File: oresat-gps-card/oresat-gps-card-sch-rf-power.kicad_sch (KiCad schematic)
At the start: 29 parts, among them U15 SKY65723-81, U16 BP2G+, U17 MAX8510EXK29+T, U18 MAX8510EXK29+T, U19 MAX8510EXK33+T

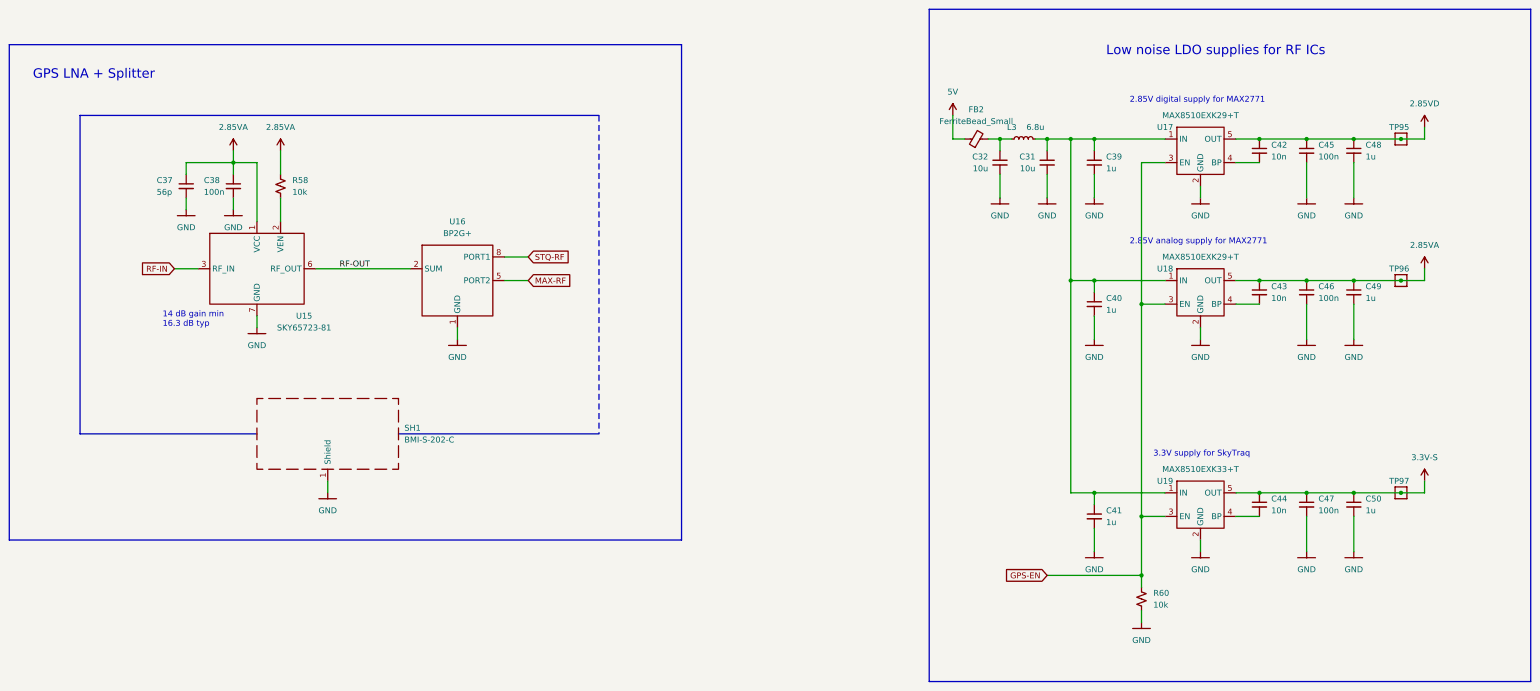
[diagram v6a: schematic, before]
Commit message: updated symbols and started new 2771 symbol
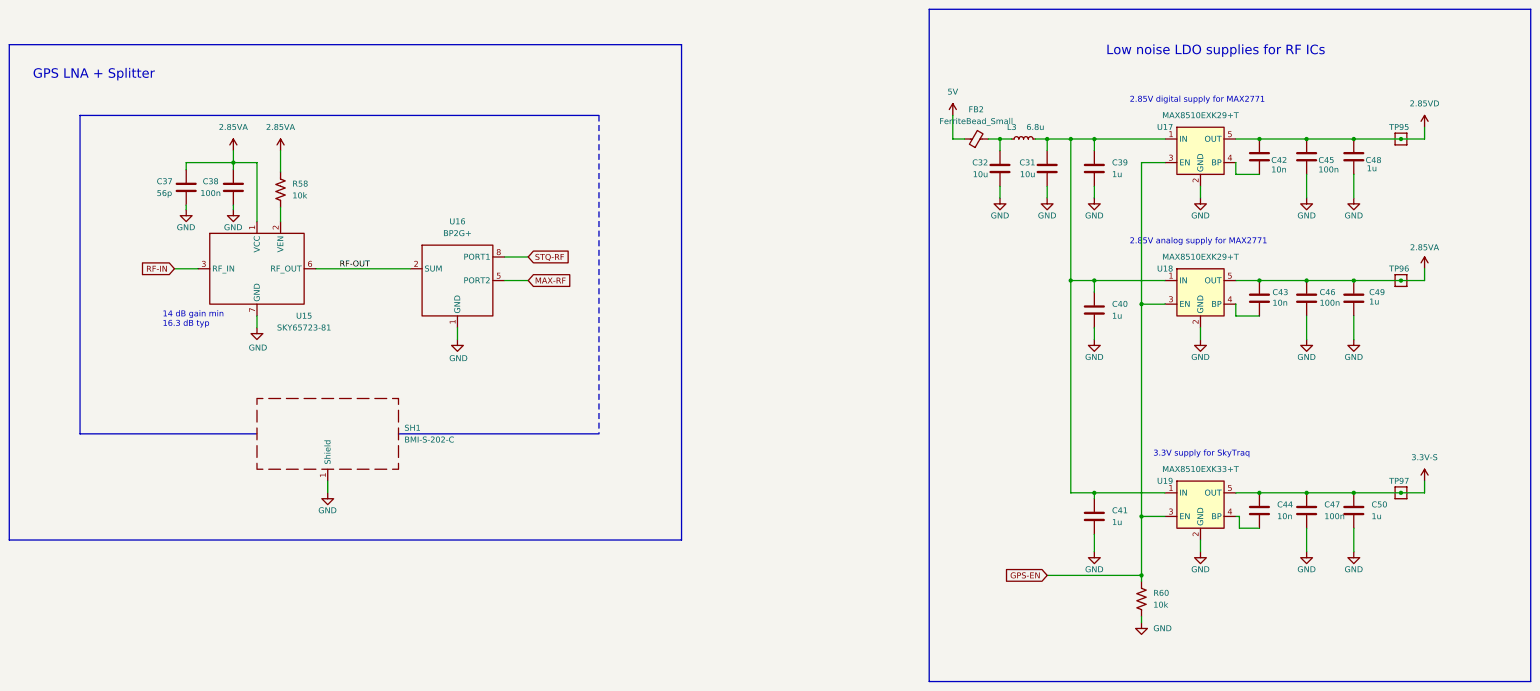
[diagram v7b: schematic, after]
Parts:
- C31, C32, C37, C38, C39, C40, C41, C42, C43, C44, C45, C46, C47, C48, C49, C50: symbol Device:C_Small -> Device:C
- R58, R60: symbol Device:R_Small_US -> Device:R_US
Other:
- moved on the sheet: C31, C32, C39, C40, C42, C43, C44, C45, C46, C47, C48, C49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
